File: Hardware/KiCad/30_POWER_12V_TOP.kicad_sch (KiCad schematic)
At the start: 0 parts

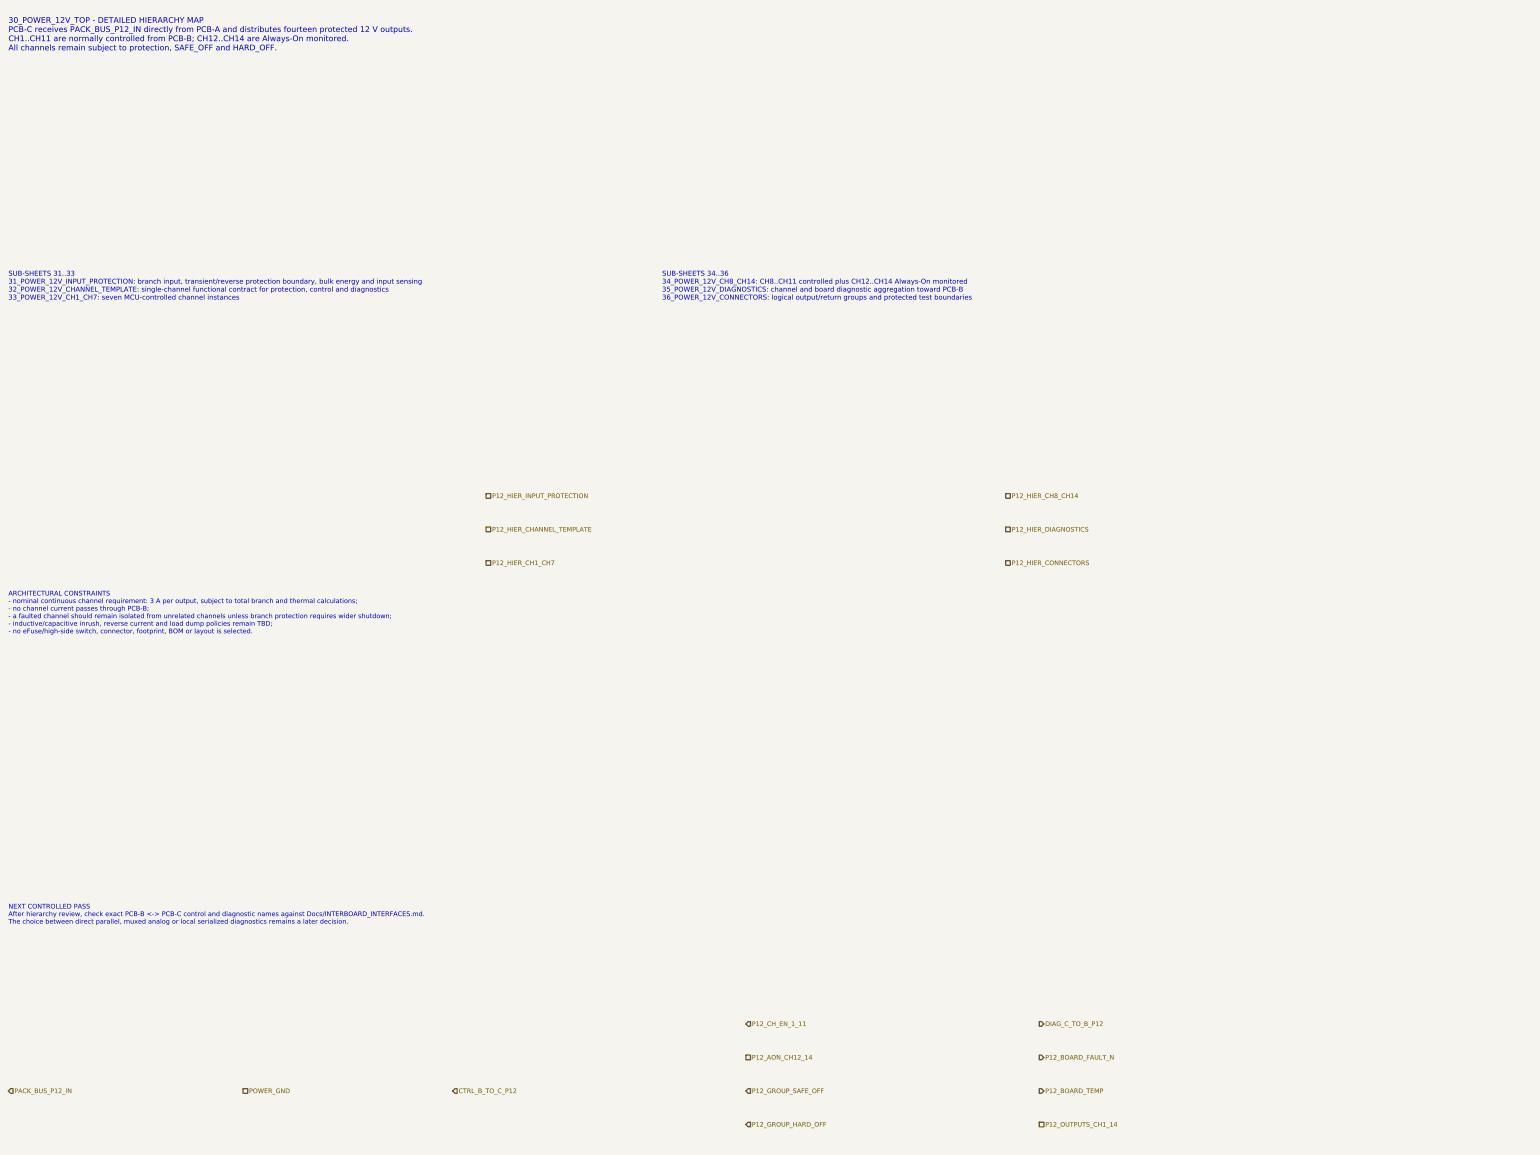
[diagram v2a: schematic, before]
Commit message: hardware: align PCB-C POWER_12V interfaces
Merge PCB-C interface consistency after verifying exact control/diagnostic buses and SAFE/HARD_OFF semantics.
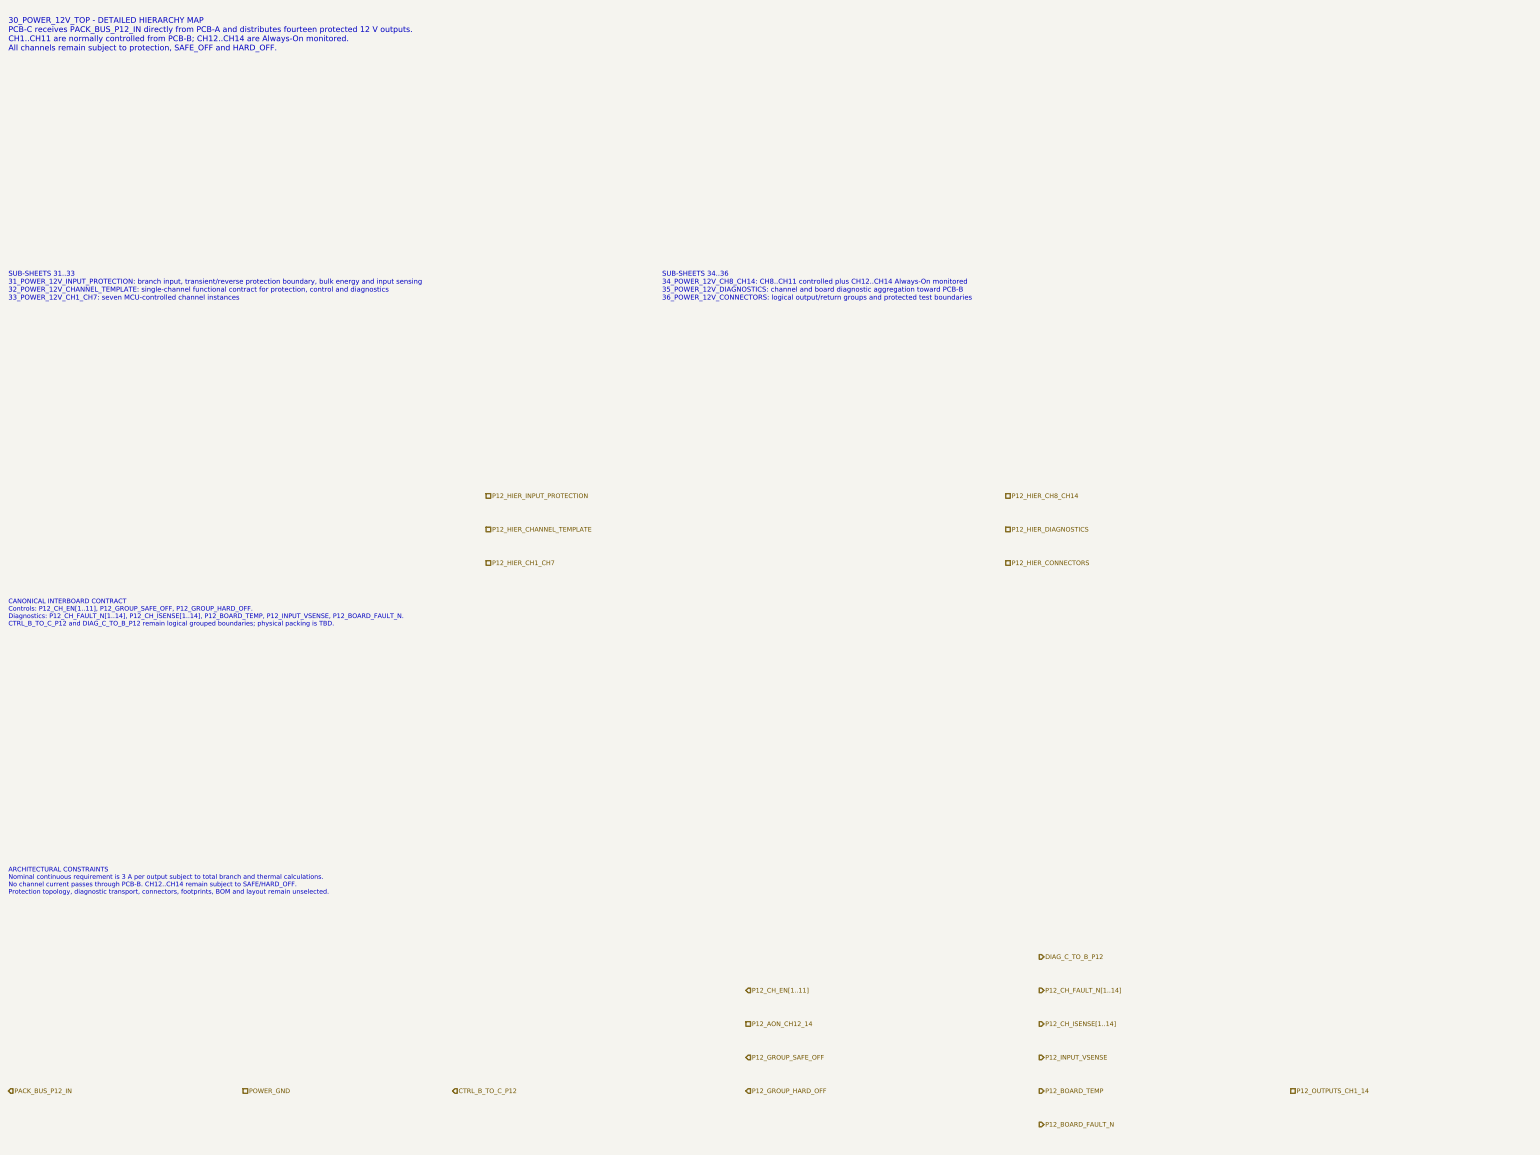
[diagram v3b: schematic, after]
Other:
- note added: "ARCHITECTURAL CONSTRAINTS Nominal continuous requirement is 3 A per output subject to total branch and thermal calculations. No channel current passes through PCB-B. CH12..CH14 remain subject to SAFE/HARD_OFF. Protection topology, diagnostic transport, connectors, footprints, BOM and layout remain unselected."
- note added: "CANONICAL INTERBOARD CONTRACT Controls: P12_CH_EN[1..11], P12_GROUP_SAFE_OFF, P12_GROUP_HARD_OFF. Diagnostics: P12_CH_FAULT_N[1..14], P12_CH_ISENSE[1..14], P12_BOARD_TEMP, P12_INPUT_VSENSE, P12_BOARD_FAULT_N. CTRL_B_TO_C_P12 and DIAG_C_TO_B_P12 remain logical grouped boundaries; physical packing is TBD."
- note removed: "ARCHITECTURAL CONSTRAINTS - nominal continuous channel requirement: 3 A per output, subject to total branch and thermal calculations; - no channel current passes through PCB-B; - a faulted channel should remain isolated from unrelated channels unless branch protection requires wider shutdown; - inductive/capacitive inrush, reverse current and load dump policies remain TBD; - no eFuse/high-side sw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"
- note removed: "NEXT CONTROLLED PASS After hierarchy review, check exact PCB-B <-> PCB-C control and diagnostic names against Docs/INTERBOARD_INTERFACES.md. The choice between direct parallel, muxed analog or local serialized diagnostics remains a later decision."
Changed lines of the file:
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@@
 		(title "30_POWER_12V_TOP - PCB-C_POWER_12V")
 		(date "2026-07-15")
-		(rev "A3")
+		(rev "A4")
 		(company "Gonoboben/plataVM")
-		(comment 1 "Architecture Level A/B: detailed hierarchy with preserved canonical boundaries")
-		(comment 2 "Sub-sheets 31..36 define functional boundaries only; no components selected")
+		(comment 1 "Interface consistency: exact PCB-B/PCB-C control and diagnostic bus names")
+		(comment 2 "Detailed hierarchy 31..36; no components, connectors or footprints selected")
 	)
 	(text "30_POWER_12V_TOP - DETAILED HIERARCHY MAP\nPCB-C receives PACK_BUS_P12_IN directly from PCB-A and distributes fourteen protected 12 V outputs.\nCH1..CH11 are normally controlled from PCB-B; CH12..CH14 are Always-On monitored.\nAll channels remain subject to protection, SAFE_OFF and HARD_OFF."
@@
 		(uuid "p12-top-00000030-0000-4000-8000-000000000103")
 	)
-	(text "ARCHITECTURAL CONSTRAINTS\n- nominal continuous channel requirement: 3 A per output, subject to total branch and thermal calculations;\n- no channel current passes through PCB-B;\n- a faulted channel should remain isolated from unrelated channels unless branch protection requires wider shutdown;\n- inductive/capacitive inrush, reverse current and load dump policies remain TBD;\n- no eFuse/high-side switch, connector, footprint, BOM or layout is selected."
+	(text "CANONICAL INTERBOARD CONTRACT\nControls: P12_CH_EN[1..11], P12_GROUP_SAFE_OFF, P12_GROUP_HARD_OFF.\nDiagnostics: P12_CH_FAULT_N[1..14], P12_CH_ISENSE[1..14], P12_BOARD_TEMP, P12_INPUT_VSENSE, P12_BOARD_FAULT_N.\nCTRL_B_TO_C_P12 and DIAG_C_TO_B_P12 remain logical grouped boundaries; physical packing is TBD."
 		(exclude_from_sim no)
 		(at 12 150 0)
-		(effects (font (size 1.12 1.12)) (justify left))
+		(effects (font (size 1.10 1.10)) (justify left))
 		(uuid "p12-top-00000030-0000-4000-8000-000000000104")
 	)
-	(text "NEXT CONTROLLED PASS\nAfter hierarchy review, check exact PCB-B <-> PCB-C control and diagnostic names against Docs/INTERBOARD_INTERFACES.md.\nThe choice between direct parallel, muxed analog or local serialized diagnostics remains a later decision."
+	(text "ARCHITECTURAL CONSTRAINTS\nNominal continuous requirement is 3 A per output subject to total branch and thermal calculations.\nNo channel current passes through PCB-B. CH12..CH14 remain subject to SAFE/HARD_OFF.\nProtection topology, diagnostic transport, connectors, footprints, BOM and layout remain unselected."
 		(exclude_from_sim no)
-		(at 12 222 0)
-		(effects (font (size 1.12 1.12)) (justify left))
+		(at 12 214 0)
+		(effects (font (size 1.10 1.10)) (justify left))
 		(uuid "p12-top-00000030-0000-4000-8000-000000000105")
 	)
@@
 	(hierarchical_label "POWER_GND" (shape passive) (exclude_from_sim no) (at 68 264 0) (effects (font (size 1.1 1.1)) (justify left)) (uuid "p12-top-00000030-0000-4000-8000-000000000208"))
 	(hierarchical_label "CTRL_B_TO_C_P12" (shape input) (exclude_from_sim no) (at 118 264 0) (effects (font (size 1.1 1.1)) (justify left)) (uuid "p12-top-00000030-0000-4000-8000-000000000209"))
-	(hierarchical_label "P12_CH_EN_1_11" (shape input) (exclude_from_sim no) (at 188 248 0) (effects (font (size 1.1 1.1)) (justify left)) (uuid "p12-top-00000030-0000-4000-8000-000000000212"))
-	(hierarchical_label "P12_AON_CH12_14" (shape passive) (exclude_from_sim no) (at 188 256 0) (effects (font (size 1.1 1.1)) (justify left)) (uuid "p12-top-00000030-0000-4000-8000-000000000213"))
-	(hierarchical_label "P12_GROUP_SAFE_OFF" (shape input) (exclude_from_sim no) (at 188 264 0) (effects (font (size 1.1 1.1)) (justify left)) (uuid "p12-top-00000030-0000-4000-8000-000000000214"))
-	(hierarchical_label "P12_GROUP_HARD_OFF" (shape input) (exclude_from_sim no) (at 188 272 0) (effects (font (size 1.1 1.1)) (justify left)) (uuid "p12-top-00000030-0000-4000-8000-000000000215"))
-	(hierarchical_label "DIAG_C_TO_B_P12" (shape output) (exclude_from_sim no) (at 258 248 0) (effects (font (size 1.1 1.1)) (justify left)) (uuid "p12-top-00000030-0000-4000-8000-000000000210"))
-	(hierarchical_label "P12_BOARD_FAULT_N" (shape output) (exclude_from_sim no) (at 258 256 0) (effects (font (size 1.1 1.1)) (justify left)) (uuid "p12-top-00000030-0000-4000-8000-000000000216"))
+	(hierarchical_label "P12_CH_EN[1..11]" (shape input) (exclude_from_sim no) (at 188 240 0) (effects (font (size 1.1 1.1)) (justify left)) (uuid "p12-top-00000030-0000-4000-8000-000000000212"))
+	(hierarchical_label "P12_AON_CH12_14" (shape passive) (exclude_from_sim no) (at 188 248 0) (effects (font (size 1.1 1.1)) (justify left)) (uuid "p12-top-00000030-0000-4000-8000-000000000213"))
+	(hierarchical_label "P12_GROUP_SAFE_OFF" (shape input) (exclude_from_sim no) (at 188 256 0) (effects (font (size 1.1 1.1)) (justify left)) (uuid "p12-top-00000030-0000-4000-8000-000000000214"))
+	(hierarchical_label "P12_GROUP_HARD_OFF" (shape input) (exclude_from_sim no) (at 188 264 0) (effects (font (size 1.1 1.1)) (justify left)) (uuid "p12-top-00000030-0000-4000-8000-000000000215"))
+	(hierarchical_label "DIAG_C_TO_B_P12" (shape output) (exclude_from_sim no) (at 258 232 0) (effects (font (size 1.1 1.1)) (justify left)) (uuid "p12-top-00000030-0000-4000-8000-000000000210"))
+	(hierarchical_label "P12_CH_FAULT_N[1..14]" (shape output) (exclude_from_sim no) (at 258 240 0) (effects (font (size 1.1 1.1)) (justify left)) (uuid "p12-top-00000030-0000-4000-8000-000000000218"))
+	(hierarchical_label "P12_CH_ISENSE[1..14]" (shape output) (exclude_from_sim no) (at 258 248 0) (effects (font (size 1.1 1.1)) (justify left)) (uuid "p12-top-00000030-0000-4000-8000-000000000219"))
+	(hierarchical_label "P12_INPUT_VSENSE" (shape output) (exclude_from_sim no) (at 258 256 0) (effects (font (size 1.1 1.1)) (justify left)) (uuid "p12-top-00000030-0000-4000-8000-000000000220"))
 	(hierarchical_label "P12_BOARD_TEMP" (shape output) (exclude_from_sim no) (at 258 264 0) (effects (font (size 1.1 1.1)) (justify left)) (uuid "p12-top-00000030-0000-4000-8000-000000000217"))
-	(hierarchical_label "P12_OUTPUTS_CH1_14" (shape passive) (exclude_from_sim no) (at 258 272 0) (effects (font (size 1.1 1.1)) (justify left)) (uuid "p12-top-00000030-0000-4000-8000-000000000211"))
+	(hierarchical_label "P12_BOARD_FAULT_N" (shape output) (exclude_from_sim no) (at 258 272 0) (effects (font (size 1.1 1.1)) (justify left)) (uuid "p12-top-00000030-0000-4000-8000-000000000216"))
+	(hierarchical_label "P12_OUTPUTS_CH1_14" (shape passive) (exclude_from_sim no) (at 318 264 0) (effects (font (size 1.1 1.1)) (justify left)) (uuid "p12-top-00000030-0000-4000-8000-000000000211"))
 )

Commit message: hardware: align PCB-C top boundary to local CAN-FD control
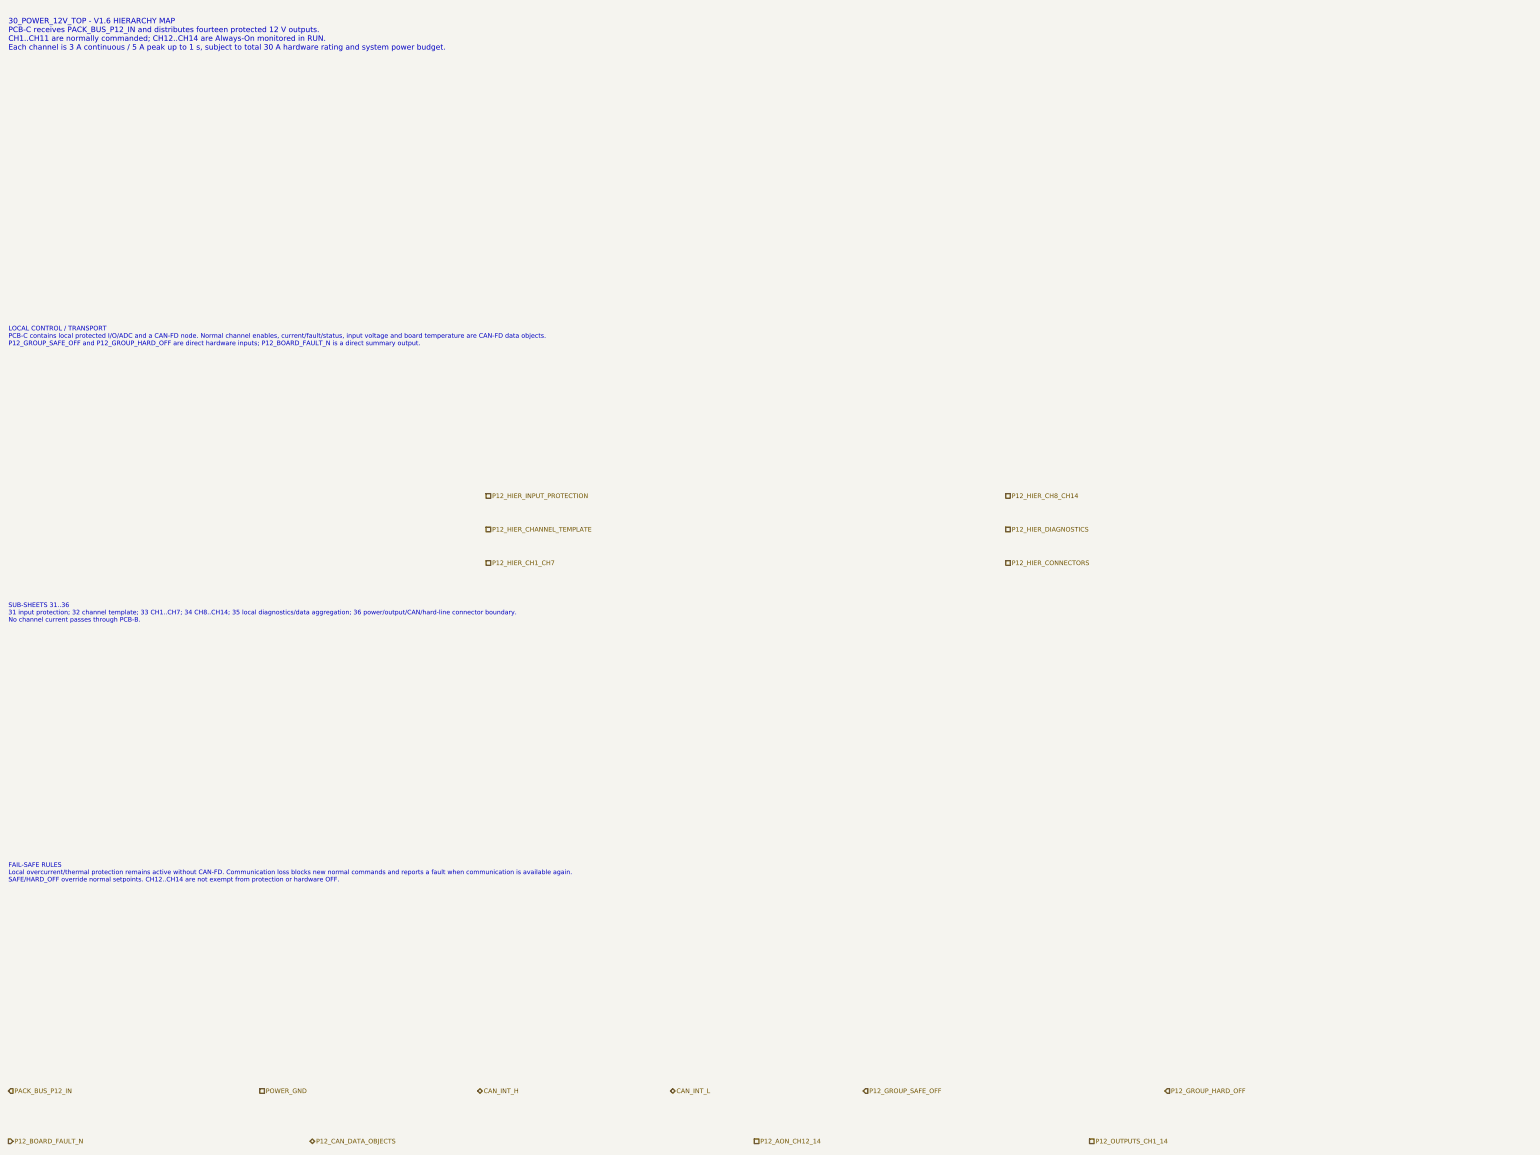
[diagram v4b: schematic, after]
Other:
- note added: "30_POWER_12V_TOP - V1.6 HIERARCHY MAP PCB-C receives PACK_BUS_P12_IN and distributes fourteen protected 12 V outputs. CH1..CH11 are normally commanded; CH12..CH14 are Always-On monitored in RUN. Each channel is 3 A continuous / 5 A peak up to 1 s, subject to total 30 A hardware rating and system power budget."
- note added: "FAIL-SAFE RULES Local overcurrent/thermal protection remains active without CAN-FD. Communication loss blocks new normal commands and reports a fault when communication is available again. SAFE/HARD_OFF override normal setpoints. CH12..CH14 are not exempt from protection or hardware OFF."
- note added: "LOCAL CONTROL / TRANSPORT PCB-C contains local protected I/O/ADC and a CAN-FD node. Normal channel enables, current/fault/status, input voltage and board temperature are CAN-FD data objects. P12_GROUP_SAFE_OFF and P12_GROUP_HARD_OFF are direct hardware inputs; P12_BOARD_FAULT_N is a direct summary output."
- note added: "SUB-SHEETS 31..36 31 input protection; 32 channel template; 33 CH1..CH7; 34 CH8..CH14; 35 local diagnostics/data aggregation; 36 power/output/CAN/hard-line connector boundary. No channel current passes through PCB-B."
- note removed: "30_POWER_12V_TOP - DETAILED HIERARCHY MAP PCB-C receives PACK_BUS_P12_IN directly from PCB-A and distributes fourteen protected 12 V outputs. CH1..CH11 are normally controlled from PCB-B; CH12..CH14 are Always-On monitored. All channels remain subject to protection, SAFE_OFF and HARD_OFF."
- note removed: "ARCHITECTURAL CONSTRAINTS Nominal continuous requirement is 3 A per output subject to total branch and thermal calculations. No channel current passes through PCB-B. CH12..CH14 remain subject to SAFE/HARD_OFF. Protection topology, diagnostic transport, connectors, footprints, BOM and layout remain unselected."
- note removed: "CANONICAL INTERBOARD CONTRACT Controls: P12_CH_EN[1..11], P12_GROUP_SAFE_OFF, P12_GROUP_HARD_OFF. Diagnostics: P12_CH_FAULT_N[1..14], P12_CH_ISENSE[1..14], P12_BOARD_TEMP, P12_INPUT_VSENSE, P12_BOARD_FAULT_N. CTRL_B_TO_C_P12 and DIAG_C_TO_B_P12 remain logical grouped boundaries; physical packing is TBD."
- note removed: "SUB-SHEETS 31..33 31_POWER_12V_INPUT_PROTECTION: branch input, transient/reverse protection boundary, bulk energy and input sensing 32_POWER_12V_CHANNEL_TEMPLATE: single-channel functional contract for protection, control and diagnostics 33_POWER_12V_CH1_CH7: seven MCU-controlled channel instances"
- note removed: "SUB-SHEETS 34..36 34_POWER_12V_CH8_CH14: CH8..CH11 controlled plus CH12..CH14 Always-On monitored 35_POWER_12V_DIAGNOSTICS: channel and board diagnostic aggregation toward PCB-B 36_POWER_12V_CONNECTORS: logical output/return groups and protected test boundaries"
